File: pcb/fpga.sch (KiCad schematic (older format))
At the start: 60 parts, among them P1 JTAG_CONN, U12 10CL025YE144C8N, U13 IS25LP016D-JBLE, U15 TLV70012, U16 TLV70025, U17 TLV70012

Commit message: Finished initial schematic with audio
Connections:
- net labels removed: HDMITX_I2S_BCK, HDMITX_I2S_DATA, HDMITX_I2S_WS
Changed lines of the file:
@@
 EESchema Schematic File Version 4
+LIBS:pcehd-cache
 EELAYER 30 0
 EELAYER END
@@
 Text Label 1650 650  0    60   ~ 0
 VCCIO
-Text HLabel 13750 5450 2    60   Output ~ 0
-HDMITX_I2S_DATA
-Text HLabel 14500 5300 0    60   Output ~ 0
-HDMITX_I2S_BCK
 Text HLabel 1700 4650 0    60   Input ~ 0
 DCK
@@
 Text HLabel 1700 2950 0    60   Input ~ 0
 A11
-Text HLabel 14500 5150 0    60   Output ~ 0
-HDMITX_I2S_WS
 Text HLabel 1700 3350 0    60   Input ~ 0
 A16

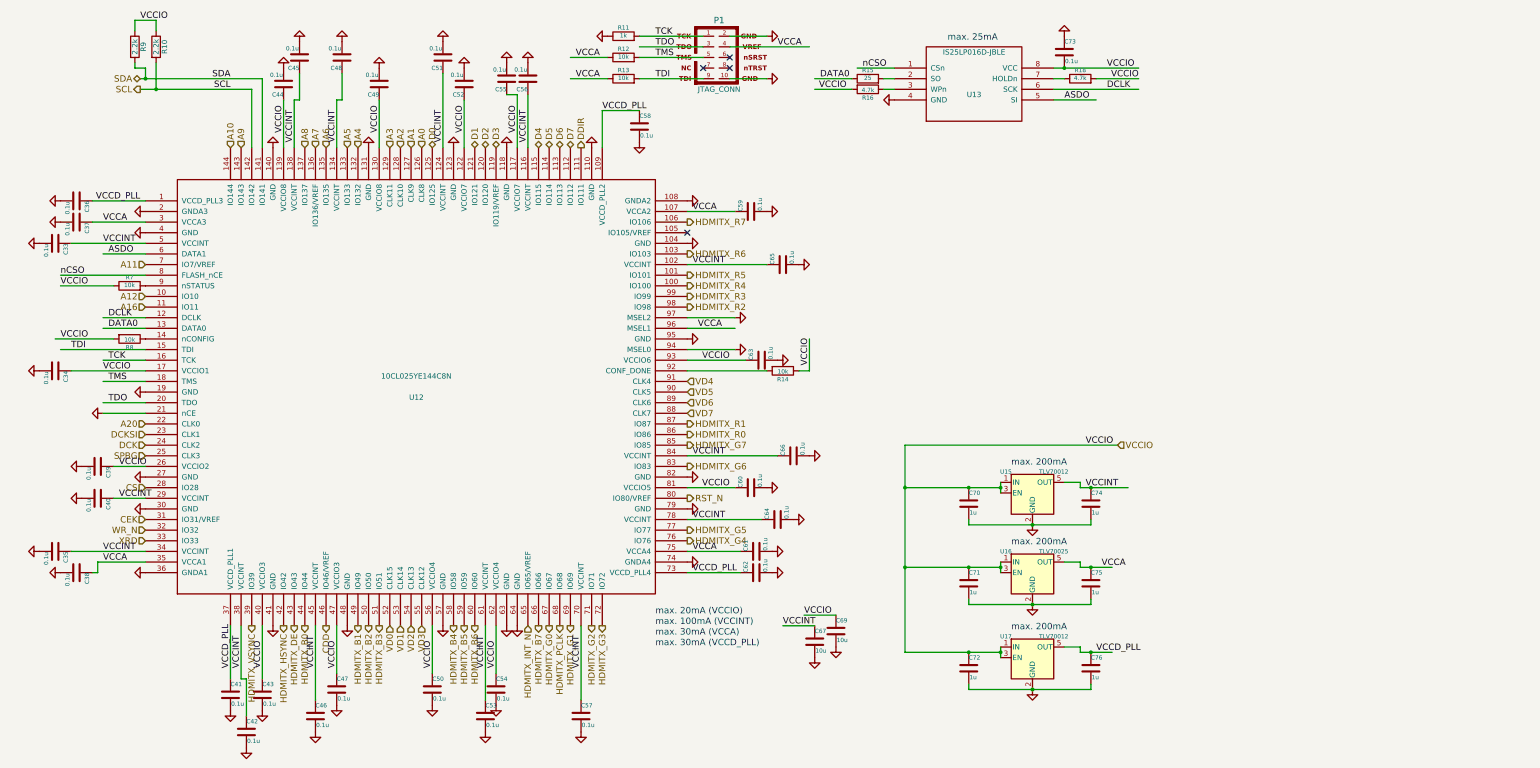
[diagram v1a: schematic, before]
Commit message: Cleaned up schematic, moved connections to busses
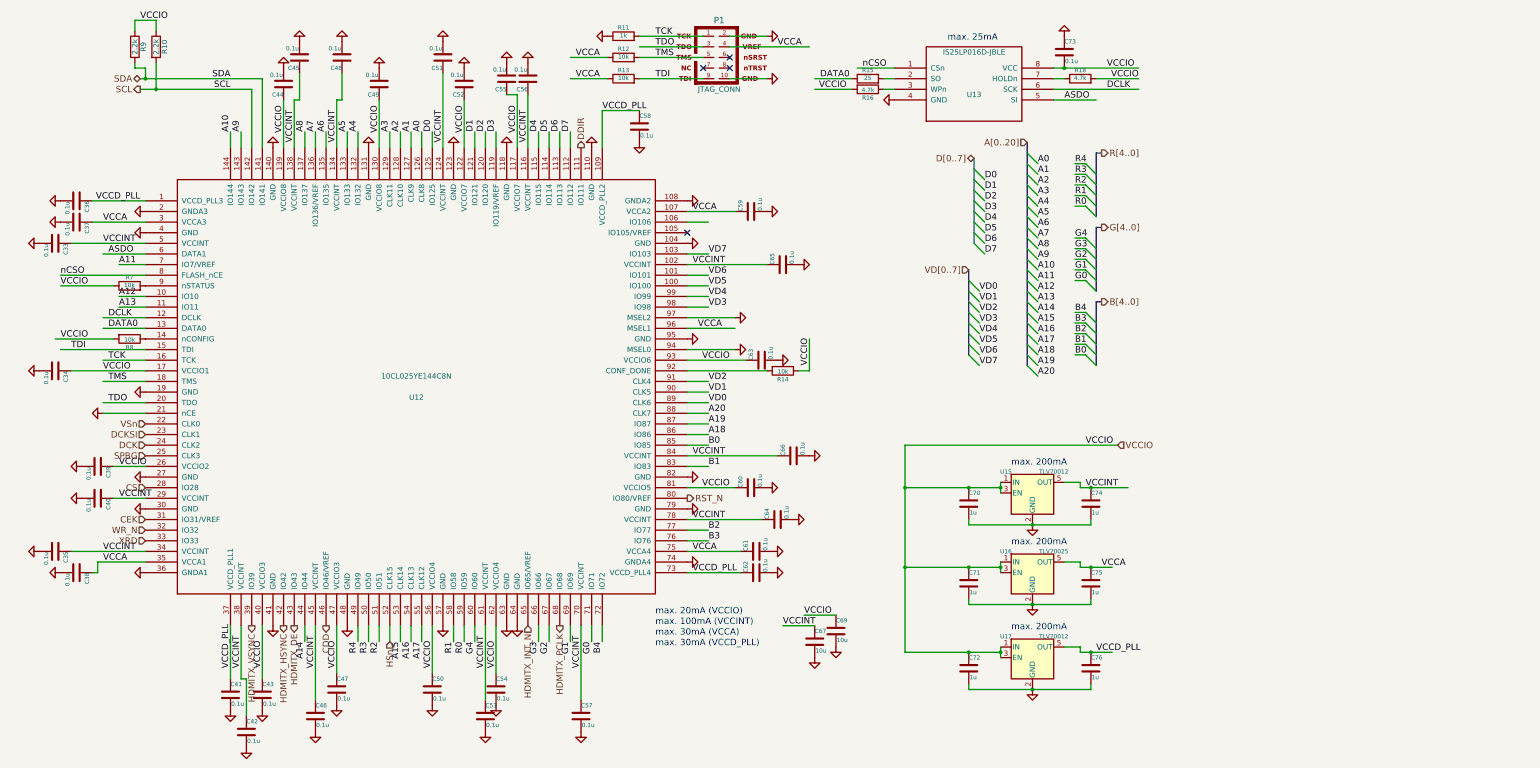
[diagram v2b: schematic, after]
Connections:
- net labels added: A13, A14, A15, A17, A18, A19, A[0..20], B0, B1, B2, B3, B4, B[4..0], D[0..7], G0, G1, G2, G3, G4, G[4..0], HSn, R0, R1, R2, R3, R4, R[4..0], VD[0..7], VSn
- net labels removed: HDMITX_B0, HDMITX_B1, HDMITX_B2, HDMITX_B3, HDMITX_B4, HDMITX_B5, HDMITX_B6, HDMITX_B7, HDMITX_G0, HDMITX_G1, HDMITX_G2, HDMITX_G3, HDMITX_G4, HDMITX_G5, HDMITX_G6, HDMITX_G7, HDMITX_R0, HDMITX_R1, HDMITX_R2, HDMITX_R3, HDMITX_R4, HDMITX_R5, HDMITX_R6, HDMITX_R7
- wire segments 136 -> 205

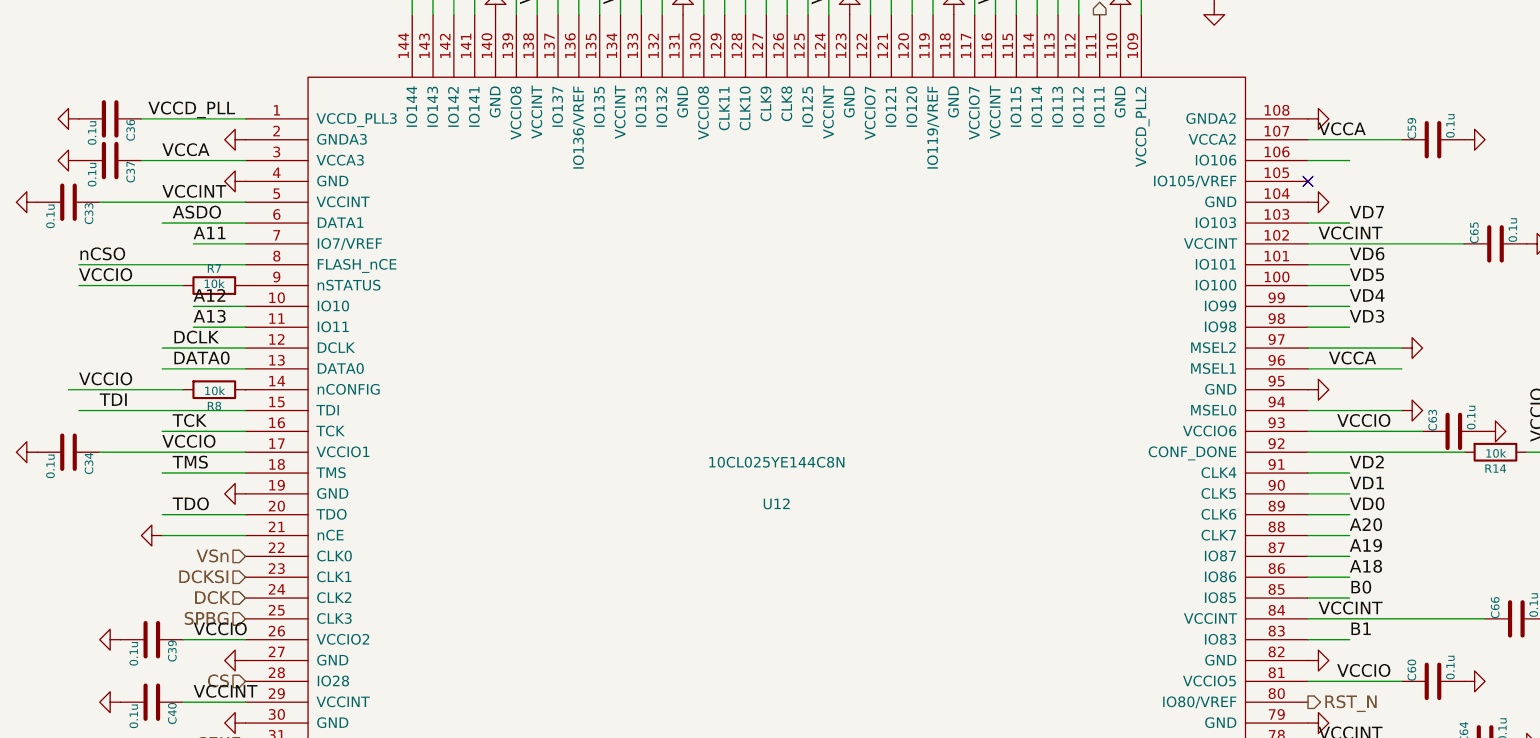
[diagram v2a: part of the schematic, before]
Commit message: Added clock selection
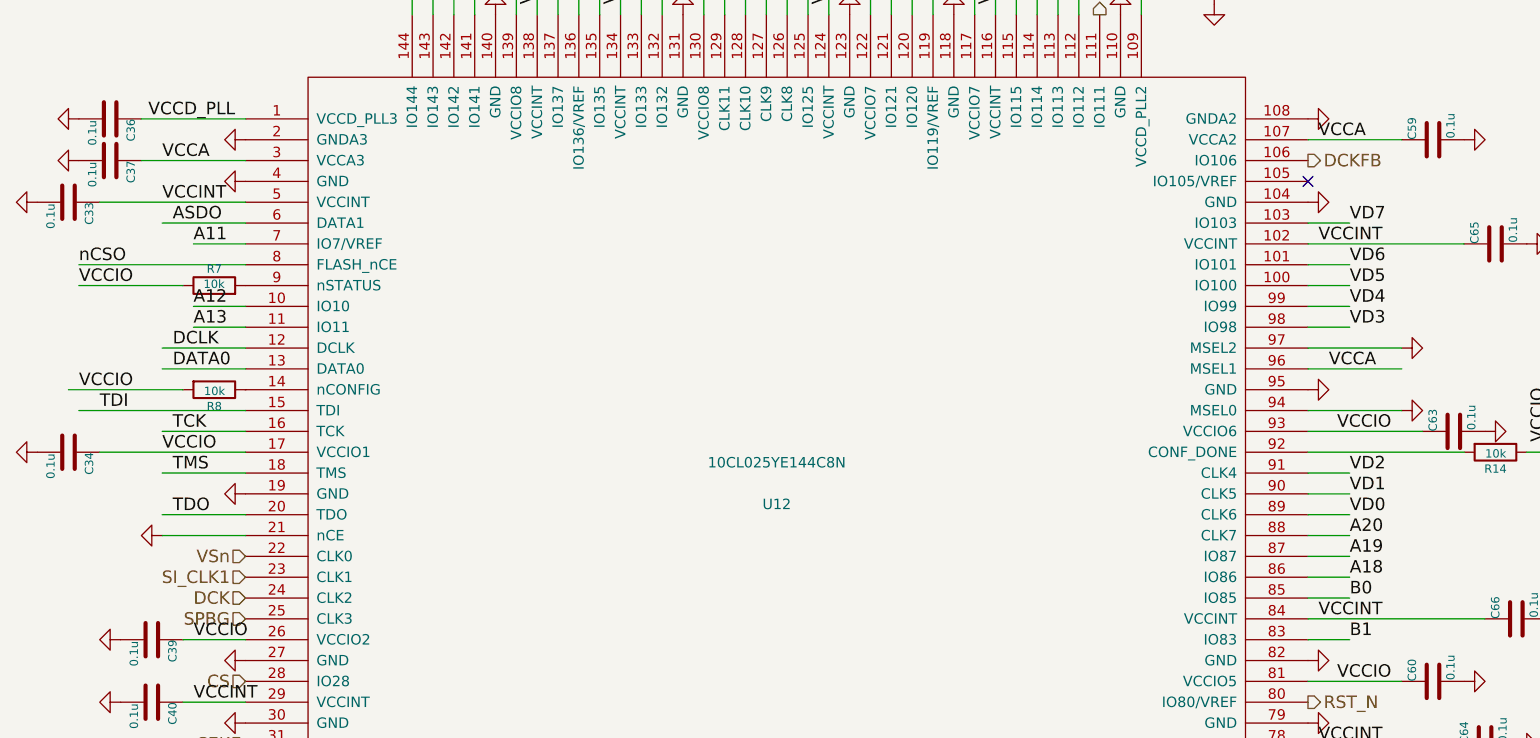
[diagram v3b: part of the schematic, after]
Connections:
- net labels added: DCKFB, SI_CLK1
- net labels removed: DCKSI
- wire segments 205 -> 204
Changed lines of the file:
@@
 EESchema Schematic File Version 4
+LIBS:pcehd-cache
 EELAYER 30 0
 EELAYER END
@@
 $EndComp
 Text HLabel 1700 4550 0    60   Input ~ 0
-DCKSI
+SI_CLK1
 Wire Wire Line
 	2800 1200 2800 1850
@@
 Text HLabel 6800 5150 2    60   Output ~ 0
 RST_N
-NoConn ~ 6800 2650
 Entry Wire Line
 	9500 2750 9600 2850
@@
 Wire Wire Line
 	6800 2850 7000 2850
-Wire Wire Line
-	6800 2550 7000 2550
 Text Label 7000 3350 0    60   ~ 0
 VD3
@@
 Text Label 7000 2850 0    60   ~ 0
 VD7
+NoConn ~ 6800 2650
+Text HLabel 6800 2550 2    60   Output ~ 0
+DCKFB
 Wire Bus Line
 	10650 1900 10650 2500

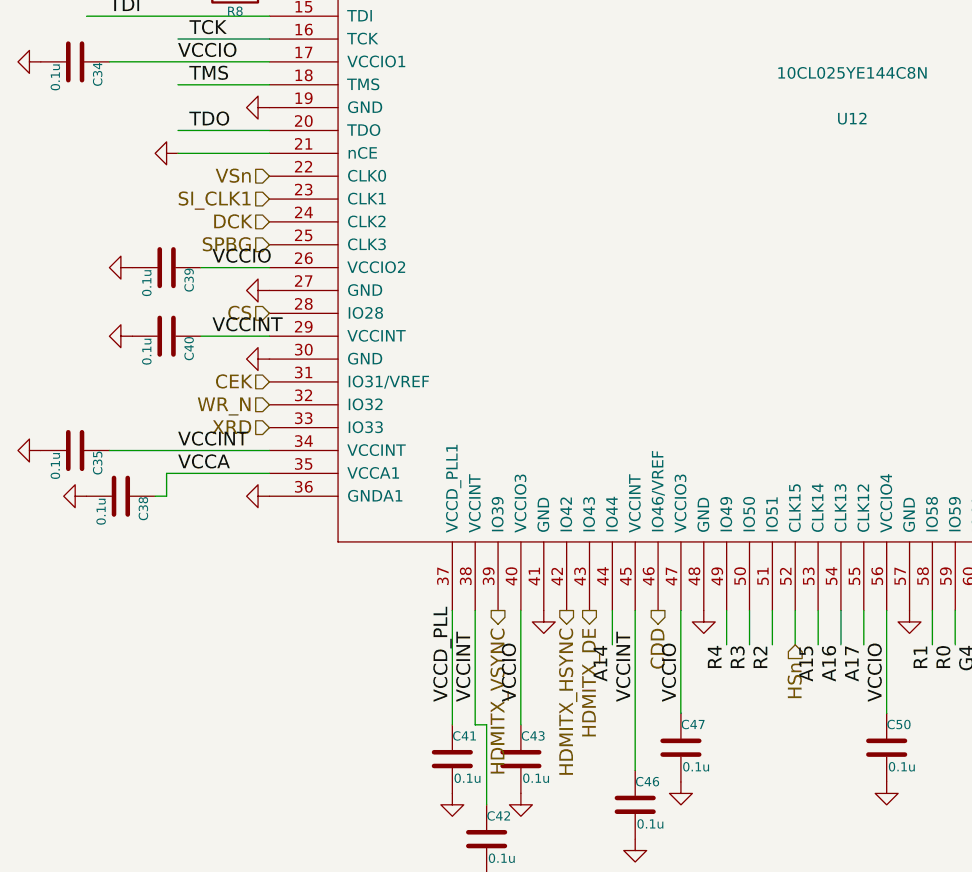
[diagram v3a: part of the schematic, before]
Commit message: Added FS7140 PLL, moved to level-shift '245
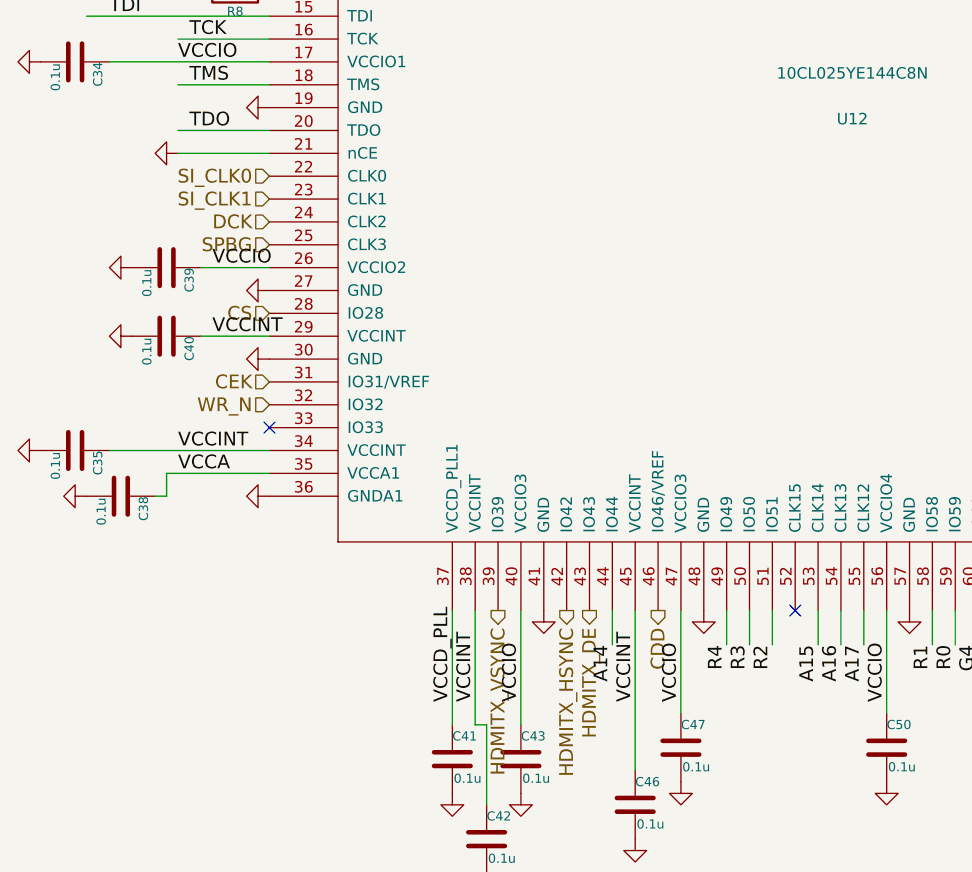
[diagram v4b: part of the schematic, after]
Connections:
- net labels added: SI_CLK0
- net labels removed: HSn, VSn, XRD
- wire segments 204 -> 203
- no-connect marks 4 -> 6
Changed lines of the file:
@@
 	-1   0    0    1
 $EndComp
-Text HLabel 1700 4550 0    60   Input ~ 0
-SI_CLK1
 Wire Wire Line
 	2800 1200 2800 1850
@@
 Wire Wire Line
 	9450 6600 9750 6600
-Text HLabel 1700 5050 0    60   Input ~ 0
-CS
 Text HLabel 1700 5350 0    60   Input ~ 0
 CEK
 Text HLabel 1700 5450 0    60   Input ~ 0
 WR_N
-Text HLabel 1700 5550 0    60   Input ~ 0
-XRD
 Text HLabel 3400 6350 3    60   Output ~ 0
 CDD
@@
 	3900 6350 3900 6500
 Wire Wire Line
-	4000 6350 4000 6500
-Wire Wire Line
 	4100 6350 4100 6500
 Wire Wire Line
@@
 Text Label 7000 4650 0    60   ~ 0
 B0
-Text HLabel 1700 4450 0    60   Input ~ 0
-VSn
-Text HLabel 4000 6500 3    60   Input ~ 0
-HSn
 Wire Wire Line
 	1700 2950 1450 2950
@@
 Text HLabel 6800 2550 2    60   Output ~ 0
 DCKFB
+Text HLabel 1700 5050 0    60   Input ~ 0
+CS
+Text HLabel 1700 4450 0    60   Input ~ 0
+SI_CLK0
+Text HLabel 1700 4550 0    60   Input ~ 0
+SI_CLK1
+NoConn ~ 4000 6350
+NoConn ~ 1700 5550
 Wire Bus Line
 	10650 1900 10650 2500

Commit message: Assigned footprints, begin layout
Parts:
- P1: footprint Connect:VASCH5x2 -> Connector_IDC:IDC-Header_2x05_P2.54mm_Vertical
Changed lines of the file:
@@
 F 0 "P1" H 7100 1350 60  0000 C CNN
 F 1 "JTAG_CONN" H 7100 700 50  0000 C CNN
-F 2 "Connect:VASCH5x2" H 7150 1000 60  0001 C CNN
+F 2 "Connector_IDC:IDC-Header_2x05_P2.54mm_Vertical" H 7150 1000 60  0001 C CNN
 F 3 "" H 7150 1000 60  0000 C CNN
 	1    7150 1000

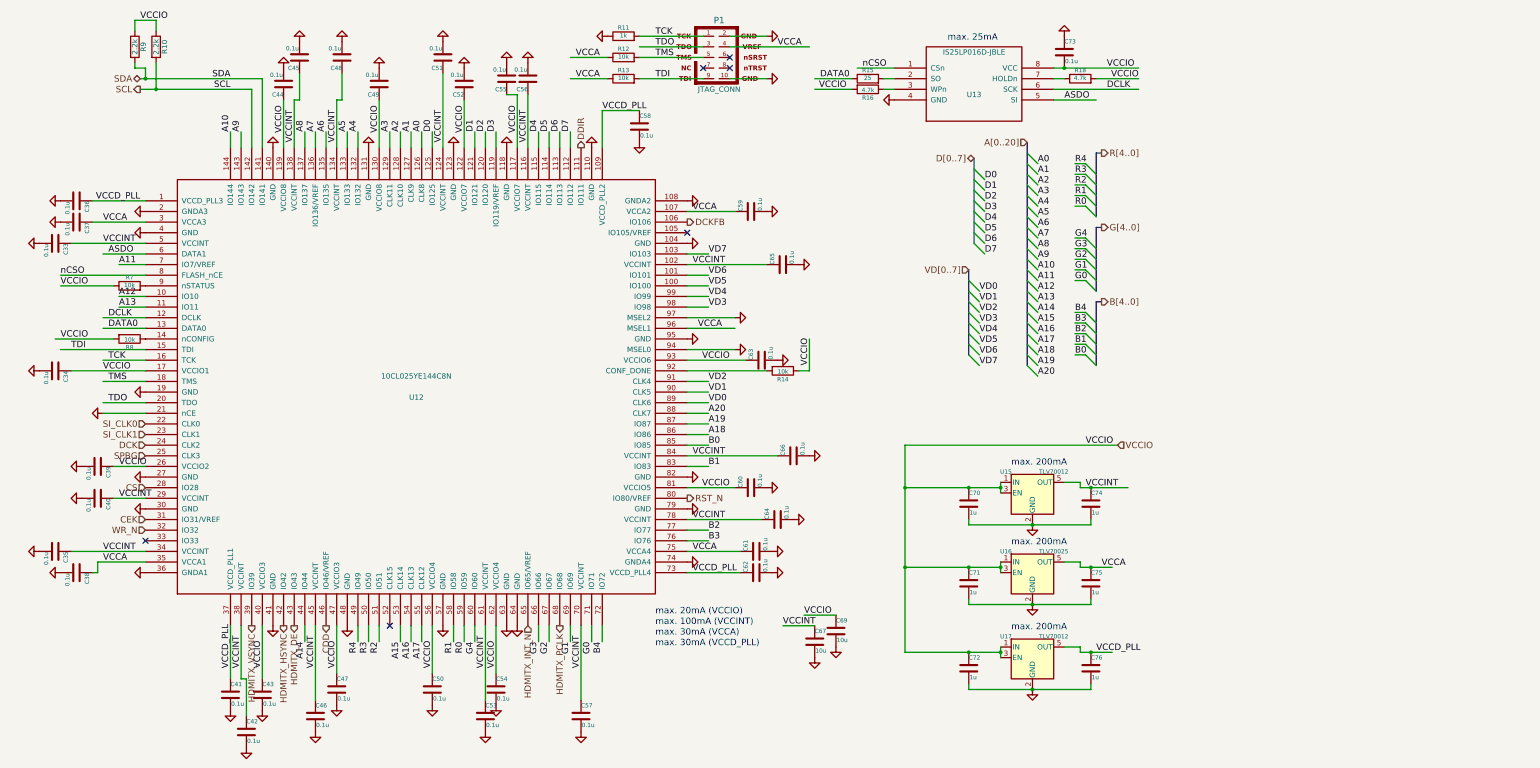
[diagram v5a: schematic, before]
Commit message: Expansion connection re-order for layout
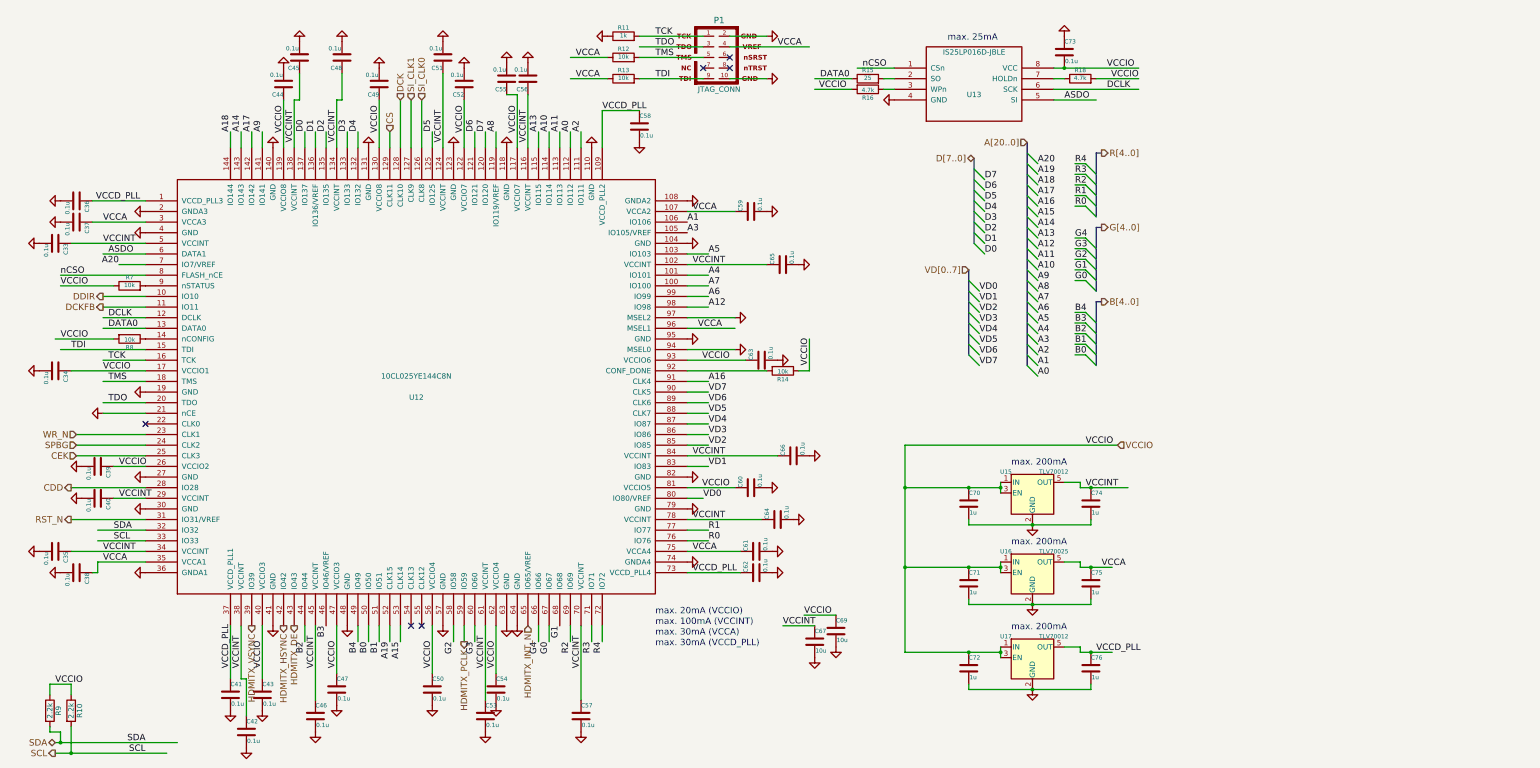
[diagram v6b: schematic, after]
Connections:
- net labels added: A[20..0], D[7..0]
- net labels removed: A[0..20], D[0..7]
- wire segments 203 -> 211
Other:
- moved on the sheet: R10, R9
